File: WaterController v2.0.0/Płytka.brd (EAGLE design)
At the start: 74.9 x 88.6 mm, 41 parts, among them IC1 DS1307ZN+, IC2 LM2576T, Q1 AOD2922, Q2 AOD2922

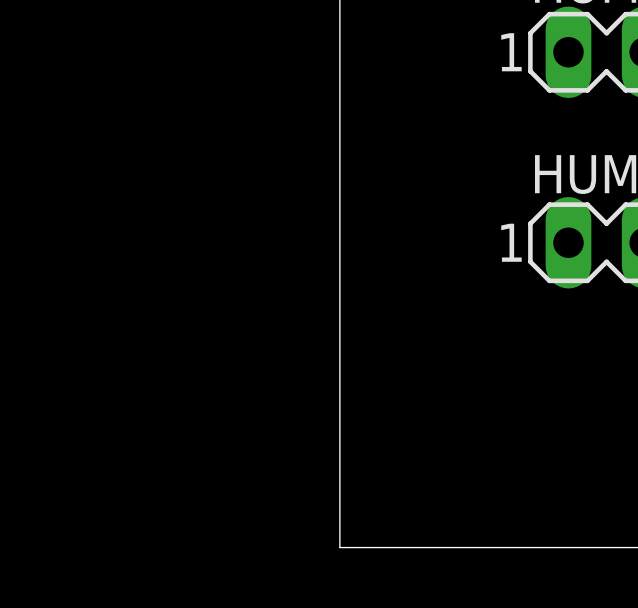
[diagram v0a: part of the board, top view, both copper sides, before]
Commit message: Add new items in PCB
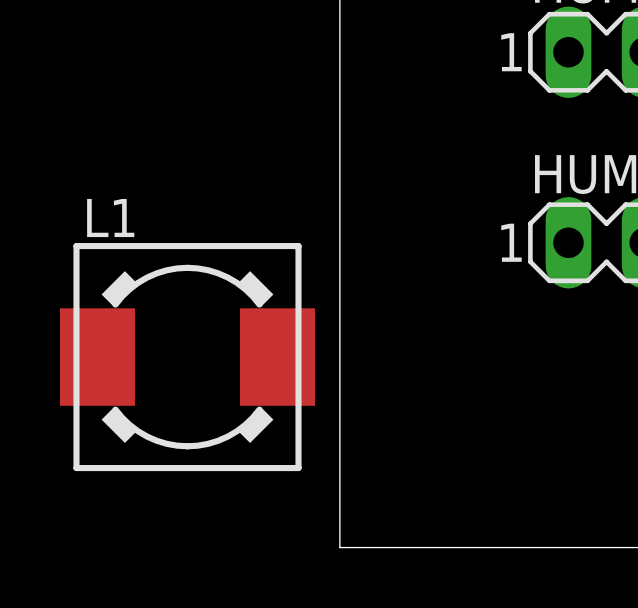
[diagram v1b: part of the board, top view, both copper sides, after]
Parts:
- added L1: DR73, inductors:DR73
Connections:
- net +5V: now also L1.2
- net N$19: now also L1.1
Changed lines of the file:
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@@
 <attribute name="VALUE" x="29.845" y="44.831" size="1.27" layer="27" ratio="10"/>
+</element>
+<element name="L1" library="inductors" library_urn="urn:adsk.eagle:library:243" package="DR73" package3d_urn="urn:adsk.eagle:package:15123/1" value="DR73" x="-1.27" y="10.16" smashed="yes">
+<attribute name="NAME" x="-4.77" y="14.16" size="1.27" layer="25"/>
+<attribute name="POPULARITY" value="0" x="-1.27" y="10.16" size="1.778" layer="27" display="off"/>
+<attribute name="SPICEPREFIX" value="L" x="-1.27" y="10.16" size="1.778" layer="27" display="off"/>
+<attribute name="VALUE" x="-4.77" y="4.66" size="1.27" layer="27"/>
 </element>
 </elements>
@@
 <contactref element="R10" pad="2"/>
 <contactref element="SV1" pad="1"/>
+<contactref element="L1" pad="2"/>
 <wire x1="66.04" y1="62.23" x2="67.31" y2="72.71" width="0" layer="19" extent="1-1"/>
 <wire x1="59.69" y1="55.56" x2="66.04" y2="62.23" width="0" layer="19" extent="1-1"/>
@@
 <wire x1="31.75" y1="38.1" x2="44.45" y2="47.31" width="0" layer="19" extent="1-1"/>
 <wire x1="25.4" y1="43.18" x2="31.75" y2="38.1" width="0" layer="19" extent="1-1"/>
-<wire x1="11.43" y1="20.32" x2="31.75" y2="38.1" width="0" layer="19" extent="1-1"/>
+<wire x1="11.43" y1="20.32" x2="25.4" y2="43.18" width="0" layer="19" extent="1-1"/>
 <wire x1="11.43" y1="13.97" x2="11.43" y2="20.32" width="0" layer="19" extent="1-1"/>
+<wire x1="1.73" y1="10.16" x2="11.43" y2="13.97" width="0" layer="19" extent="1-1"/>
 </signal>
 <signal name="A0">
@@
 <contactref element="IC2" pad="2"/>
 <contactref element="D3" pad="C"/>
+<contactref element="L1" pad="1"/>
 <wire x1="69.85" y1="12.7" x2="72.97" y2="25.83" width="0" layer="19" extent="1-1"/>
+<wire x1="-4.27" y1="10.16" x2="69.85" y2="12.7" width="0" layer="19" extent="1-1"/>
 </signal>
 <signal name="N$1">

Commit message: no message
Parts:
- removed ARDUINO_NANO1: (no value), ArduinoNanoV30:ARDUINO_NANO
- removed HUM1, HUM2, SUN, TEMP: (no value), con-lstb:MA04-1
- removed SV1: (no value), con-lstb:MA06-1
- added C10, C11, C12, C13, C6, C7, C8, C9: (no value), rcl:C0805K
- added D4, D5, D6, D7: (no value), diode:SOD80C
- added J1: HUM1, PUTRocketLab_connectors:W_TYPE_2MM_3_N
- added J2: HUM2, PUTRocketLab_connectors:W_TYPE_2MM_3_N
- added J3: TEMP, PUTRocketLab_connectors:W_TYPE_2MM_3_N
- added J4: SUN, PUTRocketLab_connectors:W_TYPE_2MM_3_N
- added LED5: (no value), led:SML0805
- added Q4, Q5: BSS138, bss138_10:SOT23
- added R14, R15, R16, R27, R28, R29: 4k7, rcl:R0805
- added R17, R18, R19, R20, R21, R22, R23, R24, R25, R26, R30: (no value), rcl:R0805
- added S1, S2: (no value), switch-omron:B3F-10XX
- added SV2: (no value), con-lstb:MA04-1
- added U1: ESP-WROOM-32, esp32:ESP-WROOM-32
- added U2: LM3940IMP-3.3, LM3940IMP-3.3:SOT230P700X180-4N
- C3, C4, C5: device capacitor-wima:C2.5-3 -> rcl:C0805K
- IC2: value LM2576T -> LM2576S/5V; device v-reg-3:TO220-5 -> v-reg-3:TO263-5
- L1: value DR73 -> DE1207-100; device inductors:DR73 -> ferrocore:DE1207
- LED1, LED2, LED3, LED4: device eagle-ltspice:LED_LD260 -> led:SML0805
- Q3: device crystal:HC49/S -> crystal:TC26H
- moved R12 144.2 mm to (-71.8, 73.0), turned to 0 degrees
- moved R9 143.5 mm to (-67.3, 83.8), turned to 0 degrees
- moved R10 135.9 mm to (-68.6, 77.5), turned to 0 degrees
- moved R7 120.4 mm to (-57.1, 83.8), turned to 0 degrees
- moved LED4 118.1 mm to (-62.2, 77.5)
- moved C5 115.1 mm to (-40.6, 77.5), turned to 0 degrees
- moved LED2 114.3 mm to (-52.1, 77.5)
- moved LED3 113.1 mm to (-57.1, 77.5)
- moved R8 112.5 mm to (-62.2, 83.8), turned to 0 degrees
- moved LED1 109.2 mm to (-47.0, 77.5)
- moved R5 109.1 mm to (-47.0, 83.8), turned to 0 degrees
- moved C4 108.4 mm to (-35.6, 77.5), turned to 0 degrees
- moved R6 108.2 mm to (-52.1, 83.8), turned to 0 degrees
- moved C3 93.3 mm to (-30.5, 77.5), turned to 0 degrees
- moved D2 88.4 mm to (-58.4, 59.7), turned to 0 degrees
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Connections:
- removed net 5V: ARDUINO_NANO1.12
- removed net C0: ARDUINO_NANO1.27, SV1.2
- removed net C1: ARDUINO_NANO1.30, SV1.3
- removed net C2: ARDUINO_NANO1.1, SV1.4
- removed net C3: ARDUINO_NANO1.2, SV1.5
- removed net TEMP: ARDUINO_NANO1.20, TEMP.2
- new net +3V3: C7.1, R14.2, R15.2, R25.2, R26.2, R27.2, R28.2, R30.2, R7.2, R8.2, R9.2, SV2.1, U1.2, U2.3
- new net A3: C11.1, D7.C, R23.2, R24.1
- new net EN: C12.2, R26.1, S1.1, S1.2, U1.3
- new net IO0: C13.2, R25.1, S2.1, S2.2, U1.25
- new net N$15: J4.2, R23.1
- new net N$18: J2.2, R19.1
- new net N$21: J3.2, R21.1
- new net N$23: LED5.A, R30.1
- new net N$4: Q4.1, R14.1
- new net N$8: Q5.1, R27.1
- new net N$9: J1.2, R18.1
- new net RX: SV2.3, U1.34
- new net SCL_LV: DISP.2, Q5.2, R28.1, U1.36
- new net SDA_LV: DISP.3, Q4.2, R15.1, U1.33
- new net TX: SV2.2, U1.35
- net +5V: now also C6.1, J1.1, J2.1, J3.1, J4.1, R16.2, R29.2, U2.1; no longer ARDUINO_NANO1.15, HUM1.1, HUM2.1, R7.2, R8.2, R9.2, SUN.1, SV1.1, TEMP.1
- net A0: now also C8.1, D4.C, R17.2, R18.2, U1.4; no longer ARDUINO_NANO1.4, HUM1.2
- net A1: now also C9.1, D5.C, R19.2, R20.1, U1.5; no longer ARDUINO_NANO1.5, HUM2.2
- net A2: now also C10.1, D6.C, R21.2, R22.1, U1.6; no longer ARDUINO_NANO1.6, SUN.2
- net GND: now also C10.2, C11.2, C12.1, C13.1, C6.2, C7.2, C8.2, C9.2, D4.A, D5.A, D6.A, D7.A, J1.3, J2.3, J3.3, J4.3, LED1.C, LED2.C, LED3.C, LED4.C, LED5.C, R17.1, R20.2, R22.2, R24.2, S1.3, S1.4, S2.3, S2.4, SV2.4, U1.1, U1.15, U1.38, U1.GND, U2.2, U2.4; no longer ARDUINO_NANO1.14, ARDUINO_NANO1.19, HUM1.4, HUM2.4, LED1.K, LED2.K, LED3.K, LED4.K, SUN.4, SV1.6, TEMP.4
- net N$1: now also U1.28; no longer ARDUINO_NANO1.21
- net N$2: now also U1.27; no longer ARDUINO_NANO1.22
- net P1: now also U1.13; no longer ARDUINO_NANO1.29
- net P1ON: now also U1.31; no longer ARDUINO_NANO1.25
- net P2: now also U1.14; no longer ARDUINO_NANO1.28
- net P2ON: now also U1.30; no longer ARDUINO_NANO1.26
- net SCL: now also Q5.3, R29.1; no longer ARDUINO_NANO1.9, DISP.2
- net SDA: now also Q4.3, R16.1; no longer ARDUINO_NANO1.8, DISP.3
- net SW: now also U1.29; no longer ARDUINO_NANO1.23
- net USBCON: no longer ARDUINO_NANO1.24
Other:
- board size 74.9 x 88.6 mm -> 97.8 x 73.3 mm

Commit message: Add new board from another project
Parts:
- removed D2: 1N4004, diode:DO41-10
- removed DISP: (no value), con-lstb:MA04-1
- removed ENCO: (no value), con-lstb:MA05-1
- removed LED2, LED3, LED4: (no value), led:SML0805
- removed POMP1, POMP2: (no value), con-ptr500:AK500/2-H
- removed R23, R24: (no value), rcl:R0805
- removed U2: LM3940IMP-3.3, LM3940IMP-3.3:SOT230P700X180-4N
- added C14, C15: 10u, rcl:C0805K
- added C16: 10u, rcl:E3,5-8
- added C17: 22u, rcl:C0805K
- added C18: 100p, rcl:C0805K
- added I2C_3V3_1, I2C_3V3_2, I2C_5V_1, I2C_5V_2: (no value), con-lstb:MA04-1
- added J5: K3, PUTRocketLab_connectors:W_TYPE_2MM_2_N
- added J6: K2, PUTRocketLab_connectors:W_TYPE_2MM_2_N
- added J7: K1, PUTRocketLab_connectors:W_TYPE_2MM_2_N
- added J8: K5, PUTRocketLab_connectors:W_TYPE_2MM_2_N
- added J9: K4, PUTRocketLab_connectors:W_TYPE_2MM_2_N
- added L2: DE1207-100, ferrocore:DE1207
- added OK1: 4N35, optocoupler:DIL06
- added Q6, Q7: BSS138, bss138_10:SOT23
- added R31, R32, R33: 10k, rcl:R0805
- added R34, R35, R36: (no value), rcl:R0805
- added SV1: (no value), con-lsta:FE05-1
- C1: value (none) -> 100u
- C2: value (none) -> 10u; device rcl:E2,5-6 -> rcl:E3,5-8
- C3, C4, C5: value (none) -> 10u
- C7: value (none) -> 100u; device rcl:C0805K -> rcl:E2,5-6
- D1: value 1N4004 -> 1N5822; device diode:DO41-10 -> diode:C4111-15
- D3: device diode:DO41-10 -> diode:C4111-15
- IC1: value DS1307ZN+ -> LM2576S; device DS1307ZN+:SOIC127P600X175-8N -> v-reg-3:TO263-5
- IC2: device v-reg-3:TO263-5 -> v-reg-3:TO220-5
- Q1, Q2: value AOD2922 -> BSS138; device transistor-power:D2PACK -> bss138_10:SOT23
- Q3: value (none) -> BSS138; device crystal:TC26H -> bss138_10:SOT23
- R10: value (none) -> 330
- R11, R12, R13, R6, R7, R8, R9: value (none) -> 10k
- R17, R20: value (none) -> 20K
- R18, R19: value (none) -> 10K
- R30: value (none) -> 100
- moved R29 230.1 mm to (5.82, 18.8), turned to 180 degrees
- moved Q5 228.3 mm to (9.58, 19.6), turned to 180 degrees
- moved C6 224.5 mm to (22.0, 51.1), flipped to the top
- moved R28 223.3 mm to (5.87, 21.0), turned to 180 degrees
- moved R16 219.1 mm to (20.5, 18.3)
- moved R15 214.2 mm to (17.7, 22.5)
- moved Q4 213.9 mm to (17.6, 19.9), turned to 180 degrees
- moved R27 213.1 mm to (9.96, 22.5)
- moved R14 206.0 mm to (21.3, 20.3)
- moved C7 194.9 mm to (45.7, 61.1), flipped to the top, turned to 0 degrees
- moved D6 185.0 mm to (7.06, 39.3), turned to 270 degrees
- moved D4 184.6 mm to (10.5, 57.1), turned to 270 degrees
- moved D7 183.9 mm to (7.04, 30.9), turned to 90 degrees
- moved D5 182.5 mm to (10.7, 46.9), turned to 270 degrees
- moved C10 176.9 mm to (8.92, 40.0), turned to 270 degrees
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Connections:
- removed net CLK: C3.1, ENCO.2, R5.2
- removed net DT: C4.1, ENCO.3, R6.2
- removed net N$15: J4.2, R23.1
- removed net P1: Q1.1, R3.2, U1.13
- removed net P1ON: R11.2, U1.31
- removed net P2: Q2.1, R4.2, U1.14
- removed net P2ON: R12.2, U1.30
- removed net SW: C5.1, ENCO.4, R9.1, U1.29
- removed net USBCON: R13.2
- new net EN_5V: R35.2, U1.13
- new net K1: Q3.2, R12.1, U1.31
- new net K2: Q1.2, R7.1, U1.30
- new net K3: Q2.2, R9.1, U1.29
- new net K4: Q7.2, R33.1, U1.28
- new net K5: Q6.2, R31.1, U1.27
- new net N$14: SV1.3, U1.10
- new net N$16: Q3.1, R11.1
- new net N$17: SV1.2, U1.11
- new net N$20: Q6.1, R13.1
- new net N$22: SV1.1, U1.12
- new net N$24: Q7.1, R32.1
- new net N$25: IC2.5, OK1.5, R34.1
- new net N$26: OK1.1, R35.1
- new net N$29: C6.2, OK1.6, R36.2
- new net N$30: IC1.4, R21.2, R22.1
- net +3V3: now also C16.+, C17.2, C18.2, I2C_3V3_1.1, I2C_3V3_2.1, J3.1, J4.1, L2.2, R11.2, R12.2, R13.2, R22.2, R31.2, R32.2, R33.2, R6.2; no longer C7.1, U2.3
- net +5V: now also I2C_5V_1.1, I2C_5V_2.1, R3.2, R4.2, R5.2; no longer C6.1, DISP.1, ENCO.1, IC1.8, J3.1, J4.1, U2.1
- net A2: now also J3.2; no longer R21.2, R22.1
- net A3: now also J4.2, U1.7; no longer R23.2, R24.1
- net GND: now also C14.2, C15.2, C16.-, C17.1, C18.1, C6.1, C7.-, D1.A, I2C_3V3_1.4, I2C_3V3_2.4, I2C_5V_1.4, I2C_5V_2.4, IC1.5, J5.2, J6.2, J7.2, J8.2, J9.2, OK1.2, OK1.4, R21.1, R36.1; no longer C6.2, C7.2, DISP.4, ENCO.5, IC1.4, IC2.5, LED2.C, LED3.C, LED4.C, Q1.3, Q2.3, R22.2, R24.2, R3.1, R4.1, U2.2, U2.4
- net N$1: now also C5.1, J5.1, Q2.3, R1.1; no longer R5.1, R7.1, U1.28
- net N$10: now also SV1.5, U1.8; no longer IC1.1, Q3.2
- net N$11: now also Q1.1, R6.1; no longer IC1.2, Q3.1
- net N$12: now also SV1.4, U1.9; no longer D1.A, POMP1.1, Q1.2
- net N$13: now also Q2.1, R8.1; no longer D2.A, POMP2.1, Q2.2
- net N$2: now also C4.1, J6.1, Q1.3, R2.1; no longer R6.1, R8.1, U1.27
- net N$21: now also D1.C, IC1.2, L2.1; no longer J3.2, R21.1
- net N$5: now also C3.1, J7.1, Q3.3, R3.1; no longer LED2.A, R11.1
- net N$6: now also C14.1, J9.1, Q7.3, R5.1; no longer LED3.A, R12.1
- net N$7: now also C15.1, J8.1, Q6.3, R4.1; no longer LED4.A, R13.1
- net SCL: now also I2C_5V_1.2, I2C_5V_2.2; no longer IC1.6, R1.1
- net SCL_LV: now also I2C_3V3_1.2, I2C_3V3_2.2; no longer DISP.2
- net SDA: now also I2C_5V_1.3, I2C_5V_2.3; no longer IC1.5, R2.1
- net SDA_LV: now also I2C_3V3_1.3, I2C_3V3_2.3; no longer DISP.3
- net VCC: now also C7.+, IC1.1, R34.2; no longer D1.C, D2.C, POMP1.2, POMP2.2
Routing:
- net +5V: track 0.00 -> 278.2 mm, vias 0 -> 3
- net +3V3: track 0.00 -> 275.6 mm, vias 0 -> 1
- net VCC: track 0.00 -> 96.9 mm
- net SCL_LV: track 0.00 -> 71.7 mm, vias 0 -> 2
- net SDA_LV: track 0.00 -> 63.6 mm, vias 0 -> 3
- net EN: track 0.00 -> 45.8 mm
- net N$19: track 0.00 -> 34.9 mm
- net EN_5V: track 0.00 -> 34.6 mm, vias 0 -> 2
- net A0: track 0.00 -> 34.3 mm
- net IO0: track 0.00 -> 31.3 mm
- net K5: track 0.00 -> 28.5 mm, vias 0 -> 2
- net N$21: track 0.00 -> 27.8 mm, vias 0 -> 1
- net A1: track 0.00 -> 26.7 mm
- net GND: track 0.00 -> 26.3 mm, vias 0 -> 55
- net A2: track 0.00 -> 25.3 mm
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- added copper zone on layer 1, net GND
- added copper zone on layer 16, net GND
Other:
- board size 97.8 x 73.3 mm -> 73.3 x 77 mm
- board text added: "Arkadiusz"
- board text added: "External ports"
- board text added: "I2C ports"
- board text added: "Kruszyński"
- board text added: "SMART HOME v1.2"
- board text added: "Sensor board"

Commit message: Create new board
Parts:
- removed C14, C15: 10u, rcl:C0805K
- removed J8: K5, PUTRocketLab_connectors:W_TYPE_2MM_2_N
- removed J9: K4, PUTRocketLab_connectors:W_TYPE_2MM_2_N
- removed R13, R31, R32, R33: 10k, rcl:R0805
- added D2, D8: (no value), diode:DO214AC
- added X1: + P2, con-ptr500:AK500/4
- Q6, Q7: value BSS138 -> AOD2922; device bss138_10:SOT23 -> Clean-Kong:TO252AA
- R4, R5: value (none) -> 10K
- moved Q6 36.1 mm to (54.8, 44.7)
- moved R4 34.3 mm to (51.8, 39.8), turned to 180 degrees
- moved R5 19.0 mm to (49.0, 33.1)
- moved Q7 18.5 mm to (54.5, 34.5)
- moved C3 17.7 mm to (62.8, 26.0)
- moved J6 17.7 mm to (66.9, 15.7)
- moved R11 17.7 mm to (57.7, 26.1)
- moved R12 17.7 mm to (57.7, 21.9)
- moved R6 17.7 mm to (57.7, 17.8)
- moved R8 17.7 mm to (57.7, 9.58)
- moved J5 17.7 mm to (66.9, 7.47)
- moved J7 17.7 mm to (66.8, 23.7)
- moved Q2 17.7 mm to (60.2, 7.54)
- moved Q3 17.7 mm to (60.3, 23.8)
- moved R1 17.7 mm to (62.8, 5.74)
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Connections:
- removed net K4: Q7.2, R33.1, U1.28
- removed net K5: Q6.2, R31.1, U1.27
- removed net N$20: Q6.1, R13.1
- removed net N$24: Q7.1, R32.1
- new net P1: Q6.1, R4.2, U1.31
- new net P2: Q7.1, R5.2, U1.30
- net +3V3: no longer R13.2, R31.2, R32.2, R33.2
- net +5V: no longer R4.2, R5.2
- net GND: now also Q6.2, Q7.2, R4.1, R5.1; no longer C14.2, C15.2, J8.2, J9.2
- net K1: now also U1.29; no longer U1.31
- net K2: now also U1.28; no longer U1.30
- net K3: now also U1.27; no longer U1.29
- net N$6: now also D2.A, Q6.3, X1.2; no longer C14.1, J9.1, Q7.3, R5.1
- net N$7: now also D8.A, Q7.3, X1.4; no longer C15.1, J8.1, Q6.3, R4.1
- net VCC: now also D2.C, D8.C, X1.1, X1.3
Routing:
- net VCC: track 96.9 -> 189.9 mm
- net GND: track 26.3 -> 75.8 mm, vias 55 -> 45
- net K5: track 28.5 -> 0.00 mm, vias 2 -> 0
- net P1: track 0.00 -> 23.0 mm
- net K4: track 21.7 -> 0.00 mm, vias 2 -> 0
- net K3: track 18.9 -> 34.3 mm
- net P2: track 0.00 -> 13.1 mm
- net +5V: track 278.2 -> 265.2 mm
- net +3V3: track 275.6 -> 265.0 mm
- net TX: track 6.28 -> 13.4 mm
- net K2: track 20.7 -> 27.2 mm
- net N$6: track 7.81 -> 13.1 mm
- net N$7: track 8.04 -> 11.2 mm
- net K1: track 23.7 -> 20.9 mm
- net N$24: track 1.73 -> 0.00 mm
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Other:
- board text added: "Smart Garden"
- board text removed: "Sensor board"

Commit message: improve board schematic
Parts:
- R22: value (none) -> 1k69
- moved C6 1.18 mm to (20.9, 50.9)
- moved R36 1.00 mm to (21.0, 52.8)
- moved R35 0.89 mm to (30.5, 52.7)
- moved L2 0.64 mm to (57.6, 60.0)
- moved D1 0.52 mm to (56.6, 51.1)
- moved Q6 0.46 mm to (55.0, 44.3)
- moved OK1 0.45 mm to (24.9, 57.8)
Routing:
- net N$29: track 6.26 -> 5.13 mm
- net N$26: track 4.69 -> 5.22 mm
- net GND: vias 45 -> 46

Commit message: correct mistakes in board
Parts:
- moved J4 2.01 mm to (2.39, 27.6)
- moved J1 1.48 mm to (2.11, 57.5)
- moved J3 0.52 mm to (2.26, 37.7)
- moved J2 0.41 mm to (2.08, 47.4)
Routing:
- net +5V: track 265.2 -> 266.9 mm
- net N$9: track 5.86 -> 5.04 mm
